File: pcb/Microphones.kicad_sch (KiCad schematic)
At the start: 36 parts, among them U1 AD8426ACPZ-R7, U2 AD8426ACPZ-R7

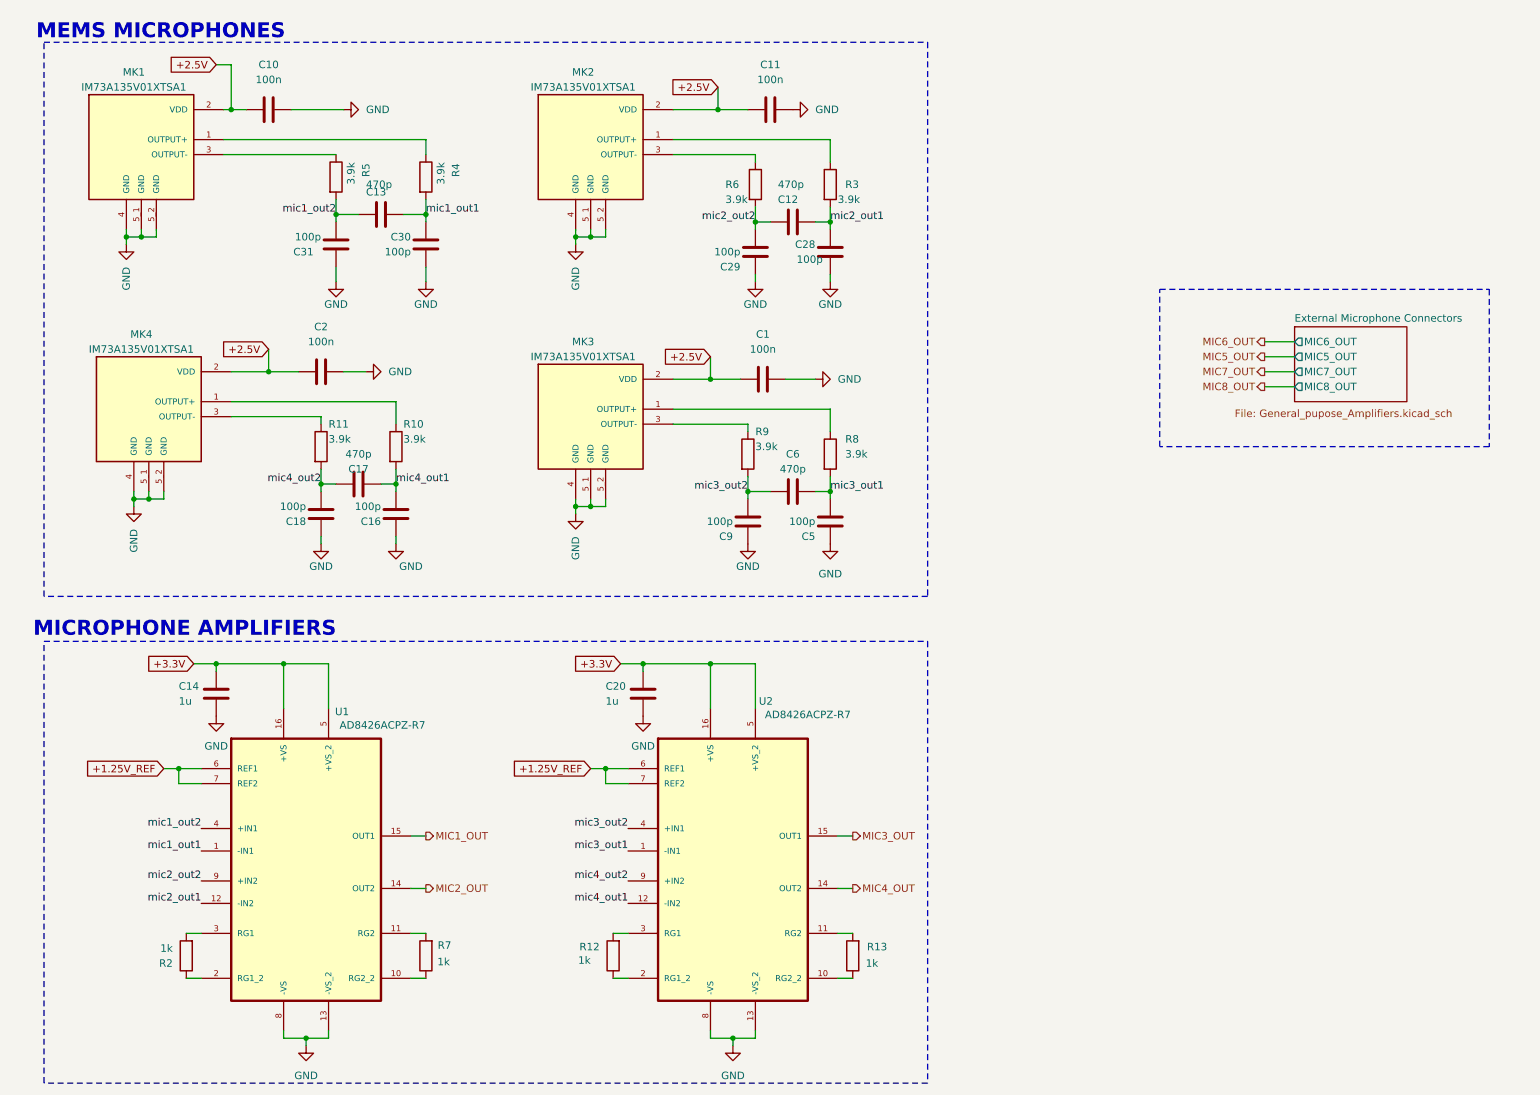
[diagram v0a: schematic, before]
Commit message: pcb: New PCB revision (#88)
- Rearrange schematics
- Better symbols and footprints
- Better names and graphics
- Add simulations for DC offset after AC coupling
- Add BOM
- Redraw PCB layout
- Proper position for pressure and humidity sensor
- Better positions for EXT headers
- Silkscreen text labels for headers, pins, mics, etc.
- Change supply polarity and pin numbers of ADA4511
- Change cap of switches to 100n to reduce BOM
- Change supply of sensors to unison 3.3V
- Rearrange ADC pins
- Add digital switches instead of manual headers
- Add logos

---------

Co-authored-by: oberfeli <felix.ober@mailbox.org>
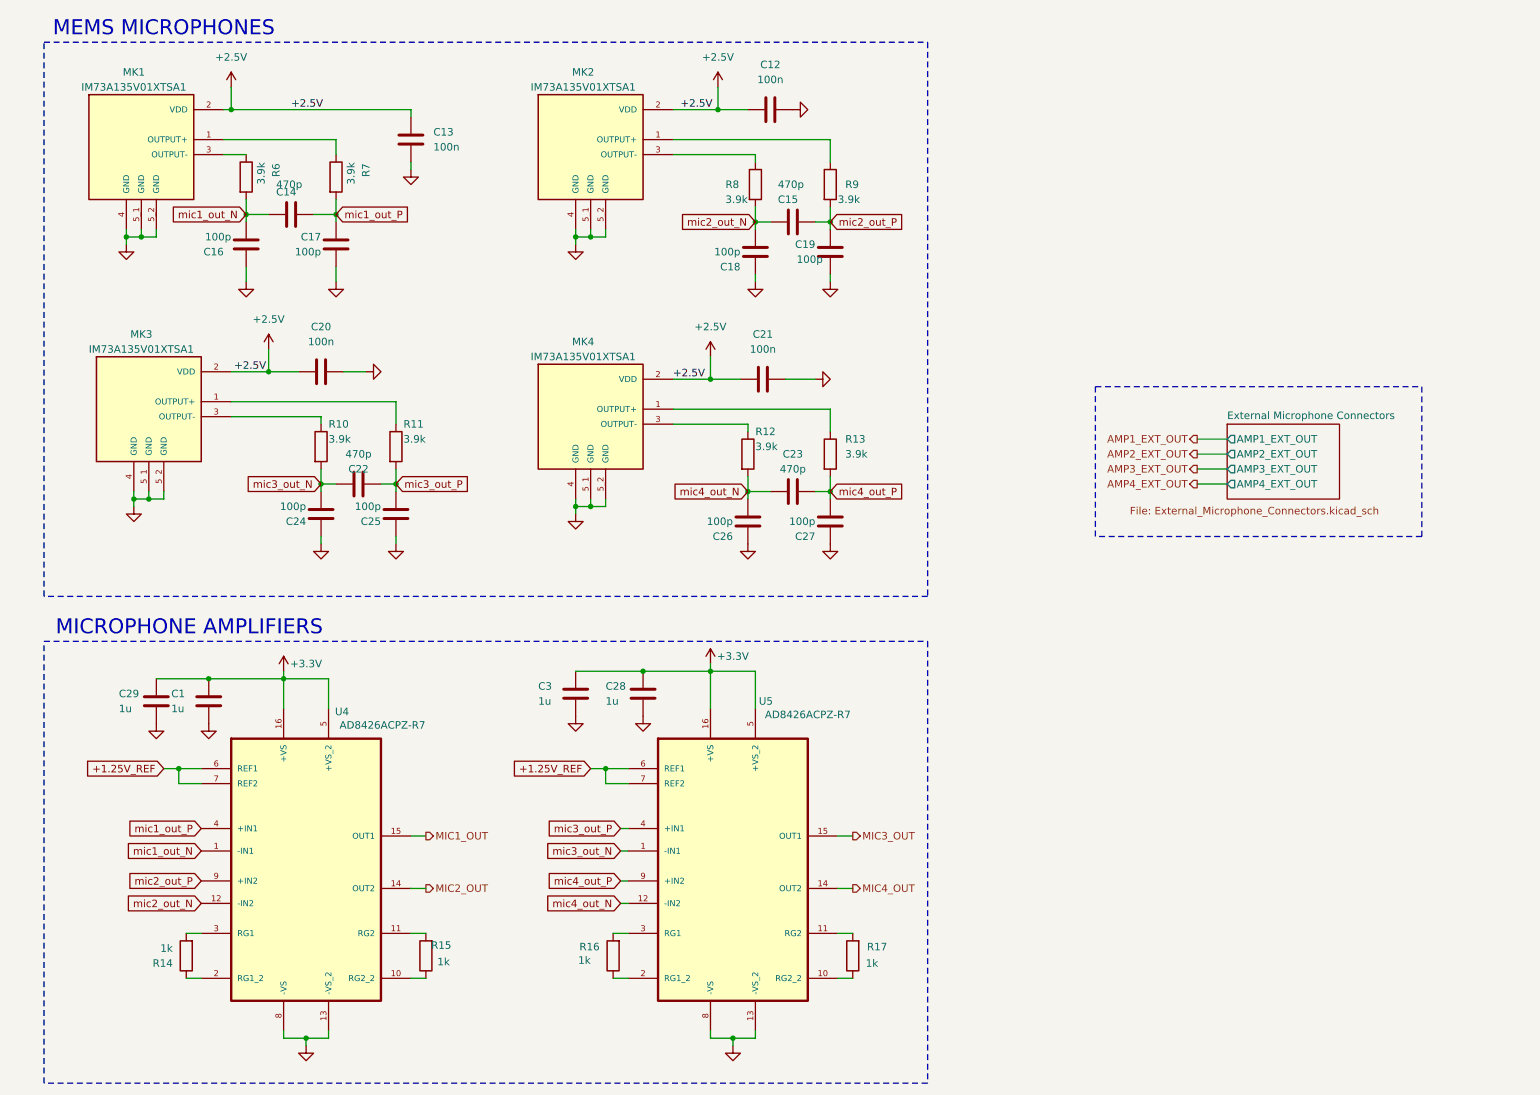
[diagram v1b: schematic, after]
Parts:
- added C1, C3: 1u, Capacitor_SMD:C_0603_1608Metric, symbol SensEdu:C
- C12: renamed from C11; footprint Capacitor_SMD:C_0805_2012Metric -> Capacitor_SMD:C_0603_1608Metric; symbol Device:C -> SensEdu:C
- C13: renamed from C10; footprint Capacitor_SMD:C_0805_2012Metric -> Capacitor_SMD:C_0603_1608Metric; symbol Device:C -> SensEdu:C
- C14: renamed from C13; footprint Capacitor_SMD:C_0805_2012Metric -> Capacitor_SMD:C_0603_1608Metric; symbol Device:C -> SensEdu:C
- C15: renamed from C12; footprint Capacitor_SMD:C_0805_2012Metric -> Capacitor_SMD:C_0603_1608Metric; symbol Device:C -> SensEdu:C
- C16: renamed from C31; footprint Capacitor_SMD:C_0805_2012Metric -> Capacitor_SMD:C_0603_1608Metric; symbol Device:C -> SensEdu:C
- C17: renamed from C30; footprint Capacitor_SMD:C_0805_2012Metric -> Capacitor_SMD:C_0603_1608Metric; symbol Device:C -> SensEdu:C
- C18: renamed from C29; footprint Capacitor_SMD:C_0805_2012Metric -> Capacitor_SMD:C_0603_1608Metric; symbol Device:C -> SensEdu:C
- C19: renamed from C28; footprint Capacitor_SMD:C_0805_2012Metric -> Capacitor_SMD:C_0603_1608Metric; symbol Device:C -> SensEdu:C
- C20: renamed from C2; footprint Capacitor_SMD:C_0805_2012Metric -> Capacitor_SMD:C_0603_1608Metric; symbol Device:C -> SensEdu:C
- C21: renamed from C1; footprint Capacitor_SMD:C_0805_2012Metric -> Capacitor_SMD:C_0603_1608Metric; symbol Device:C -> SensEdu:C
- C22: renamed from C17; footprint Capacitor_SMD:C_0805_2012Metric -> Capacitor_SMD:C_0603_1608Metric; symbol Device:C -> SensEdu:C
- C23: renamed from C6; footprint Capacitor_SMD:C_0805_2012Metric -> Capacitor_SMD:C_0603_1608Metric; symbol Device:C -> SensEdu:C
- C24: renamed from C18; footprint Capacitor_SMD:C_0805_2012Metric -> Capacitor_SMD:C_0603_1608Metric; symbol Device:C -> SensEdu:C
- C25: renamed from C16; footprint Capacitor_SMD:C_0805_2012Metric -> Capacitor_SMD:C_0603_1608Metric; symbol Device:C -> SensEdu:C
- C26: renamed from C9; footprint Capacitor_SMD:C_0805_2012Metric -> Capacitor_SMD:C_0603_1608Metric; symbol Device:C -> SensEdu:C
- C27: renamed from C5; footprint Capacitor_SMD:C_0805_2012Metric -> Capacitor_SMD:C_0603_1608Metric; symbol Device:C -> SensEdu:C
- C28: renamed from C20; footprint Capacitor_SMD:C_0805_2012Metric -> Capacitor_SMD:C_0603_1608Metric; symbol Device:C -> SensEdu:C
- C29: renamed from C14; footprint Capacitor_SMD:C_0805_2012Metric -> Capacitor_SMD:C_0603_1608Metric; symbol Device:C -> SensEdu:C
- MK1, MK2: footprint MIC_IM73A135V01XTSA1 -> SensEdu:MIC_IM73A135V01XTSA1
- MK3: renamed from MK4; footprint MIC_IM73A135V01XTSA1 -> SensEdu:MIC_IM73A135V01XTSA1
- MK4: renamed from MK3; footprint MIC_IM73A135V01XTSA1 -> SensEdu:MIC_IM73A135V01XTSA1
- R10: renamed from R11; footprint Resistor_SMD:R_0805_2012Metric -> Resistor_SMD:R_0603_1608Metric; symbol Device:R -> SensEdu:R
- R11: renamed from R10; footprint Resistor_SMD:R_0805_2012Metric -> Resistor_SMD:R_0603_1608Metric; symbol Device:R -> SensEdu:R
- R12: renamed from R9; footprint Resistor_SMD:R_0805_2012Metric -> Resistor_SMD:R_0603_1608Metric; symbol Device:R -> SensEdu:R
- R13: renamed from R8; footprint Resistor_SMD:R_0805_2012Metric -> Resistor_SMD:R_0603_1608Metric; symbol Device:R -> SensEdu:R
- R14: renamed from R2; footprint Resistor_SMD:R_0805_2012Metric -> Resistor_SMD:R_0603_1608Metric; symbol Device:R -> SensEdu:R
- R15: renamed from R7; footprint Resistor_SMD:R_0805_2012Metric -> Resistor_SMD:R_0603_1608Metric; symbol Device:R -> SensEdu:R
- R16: renamed from R12; footprint Resistor_SMD:R_0805_2012Metric -> Resistor_SMD:R_0603_1608Metric; symbol Device:R -> SensEdu:R
- R17: renamed from R13; footprint Resistor_SMD:R_0805_2012Metric -> Resistor_SMD:R_0603_1608Metric; symbol Device:R -> SensEdu:R
- R6: renamed from R5; footprint Resistor_SMD:R_0805_2012Metric -> Resistor_SMD:R_0603_1608Metric; symbol Device:R -> SensEdu:R
- R7: renamed from R4; footprint Resistor_SMD:R_0805_2012Metric -> Resistor_SMD:R_0603_1608Metric; symbol Device:R -> SensEdu:R
- R8: renamed from R6; footprint Resistor_SMD:R_0805_2012Metric -> Resistor_SMD:R_0603_1608Metric; symbol Device:R -> SensEdu:R
- R9: renamed from R3; footprint Resistor_SMD:R_0805_2012Metric -> Resistor_SMD:R_0603_1608Metric; symbol Device:R -> SensEdu:R
- U5: renamed from U2; symbol SensEdu:AD8426ACPZ-R7 -> SensEdu:AD8426ACPZ-R7_1
- renumbered U1 to U4
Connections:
- net +3.3V: now also C1.1, C3.1
- net GND: now also C1.2, C3.2
- net mic1_out1 renamed mic1_out_P
- net mic1_out_P: now also U4.4 (+IN1); no longer U4.1 (-IN1)
- net mic1_out2 renamed mic1_out_N
- net mic1_out_N: now also U4.1 (-IN1); no longer U4.4 (+IN1)
- net mic2_out1 renamed mic2_out_P
- net mic2_out_P: now also U4.9 (+IN2); no longer U4.12 (-IN2)
- net mic2_out2 renamed mic2_out_N
- net mic2_out_N: now also U4.12 (-IN2); no longer U4.9 (+IN2)
- net mic3_out1 renamed mic4_out_P
- net mic4_out_P: now also U5.9 (+IN2); no longer U5.1 (-IN1)
- net mic3_out2 renamed mic4_out_N
- net mic4_out_N: now also U5.12 (-IN2); no longer U5.4 (+IN1)
- net mic4_out1 renamed mic3_out_P
- net mic3_out_P: now also U5.4 (+IN1); no longer U5.12 (-IN2)
- net mic4_out2 renamed mic3_out_N
- net mic3_out_N: now also U5.1 (-IN1); no longer U5.9 (+IN2)
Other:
- sheet External Microphone Connectors: file General_pupose_Amplifiers.kicad_sch -> External_Microphone_Connectors.kicad_sch
- sheet External Microphone Connectors ports: added AMP1_EXT_OUT, AMP2_EXT_OUT, AMP3_EXT_OUT, AMP4_EXT_OUT; removed MIC5_OUT, MIC6_OUT, MIC7_OUT, MIC8_OUT
- title: SensEdu 0.7 -> SensEdu
- moved on the sheet: C13, C14, C16, C17, C29, R6, R7

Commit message: feat: Prepare 0.9 PCB with fixed issues from 0.8 tests (#102)
* feat: Upgrade speaker simulation to realistic one

* feat: Improve PCB design after tests of rev 0.8

- Added new generation of humidity sensor
- New silkscreen information for different components
- Added additional testpoints
- Removed PWM path for ultrasound transmitter

* refactor: cleanup of symbol and footprint library

- removed components that are not used anymore
- ran final DRC to prepare for manufacturing

* feat: Update BOM with extra res, caps, tps and sht

* fix: Rename schematics to match the docs
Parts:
- C10: renamed from C12; footprint Capacitor_SMD:C_0603_1608Metric -> SensEdu:C_0603_1608Metric
- C11: renamed from C13; footprint Capacitor_SMD:C_0603_1608Metric -> SensEdu:C_0603_1608Metric
- C12: renamed from C14; footprint Capacitor_SMD:C_0603_1608Metric -> SensEdu:C_0603_1608Metric
- C13: renamed from C15; footprint Capacitor_SMD:C_0603_1608Metric -> SensEdu:C_0603_1608Metric
- C14: renamed from C16; footprint Capacitor_SMD:C_0603_1608Metric -> SensEdu:C_0603_1608Metric
- C15: renamed from C17; footprint Capacitor_SMD:C_0603_1608Metric -> SensEdu:C_0603_1608Metric
- C16: renamed from C18; footprint Capacitor_SMD:C_0603_1608Metric -> SensEdu:C_0603_1608Metric
- C17: renamed from C19; footprint Capacitor_SMD:C_0603_1608Metric -> SensEdu:C_0603_1608Metric
- C18: renamed from C20; footprint Capacitor_SMD:C_0603_1608Metric -> SensEdu:C_0603_1608Metric
- C19: renamed from C21; footprint Capacitor_SMD:C_0603_1608Metric -> SensEdu:C_0603_1608Metric
- C20: renamed from C22; footprint Capacitor_SMD:C_0603_1608Metric -> SensEdu:C_0603_1608Metric
- C21: renamed from C23; footprint Capacitor_SMD:C_0603_1608Metric -> SensEdu:C_0603_1608Metric
- C22: renamed from C24; footprint Capacitor_SMD:C_0603_1608Metric -> SensEdu:C_0603_1608Metric
- C23: renamed from C25; footprint Capacitor_SMD:C_0603_1608Metric -> SensEdu:C_0603_1608Metric
- C24: renamed from C26; footprint Capacitor_SMD:C_0603_1608Metric -> SensEdu:C_0603_1608Metric
- C25: renamed from C27; footprint Capacitor_SMD:C_0603_1608Metric -> SensEdu:C_0603_1608Metric
- C26: renamed from C3; footprint Capacitor_SMD:C_0603_1608Metric -> SensEdu:C_0603_1608Metric
- C27: renamed from C28; footprint Capacitor_SMD:C_0603_1608Metric -> SensEdu:C_0603_1608Metric
- C28: renamed from C29; footprint Capacitor_SMD:C_0603_1608Metric -> SensEdu:C_0603_1608Metric
- C29: renamed from C1; footprint Capacitor_SMD:C_0603_1608Metric -> SensEdu:C_0603_1608Metric
- R10, R11, R12, R13, R14, R15, R16, R17, R6, R7, R8, R9: footprint Resistor_SMD:R_0603_1608Metric -> SensEdu:R_0603_1608Metric
